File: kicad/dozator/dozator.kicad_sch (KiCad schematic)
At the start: 11 parts, among them J2 LCD: GND 5V SDA SCL, J3 HX711: 5V GND DOUT SCK, SW1 Encoder EC11 H15, U1 Mini-360 5V, U2 DRV8871 MODULE

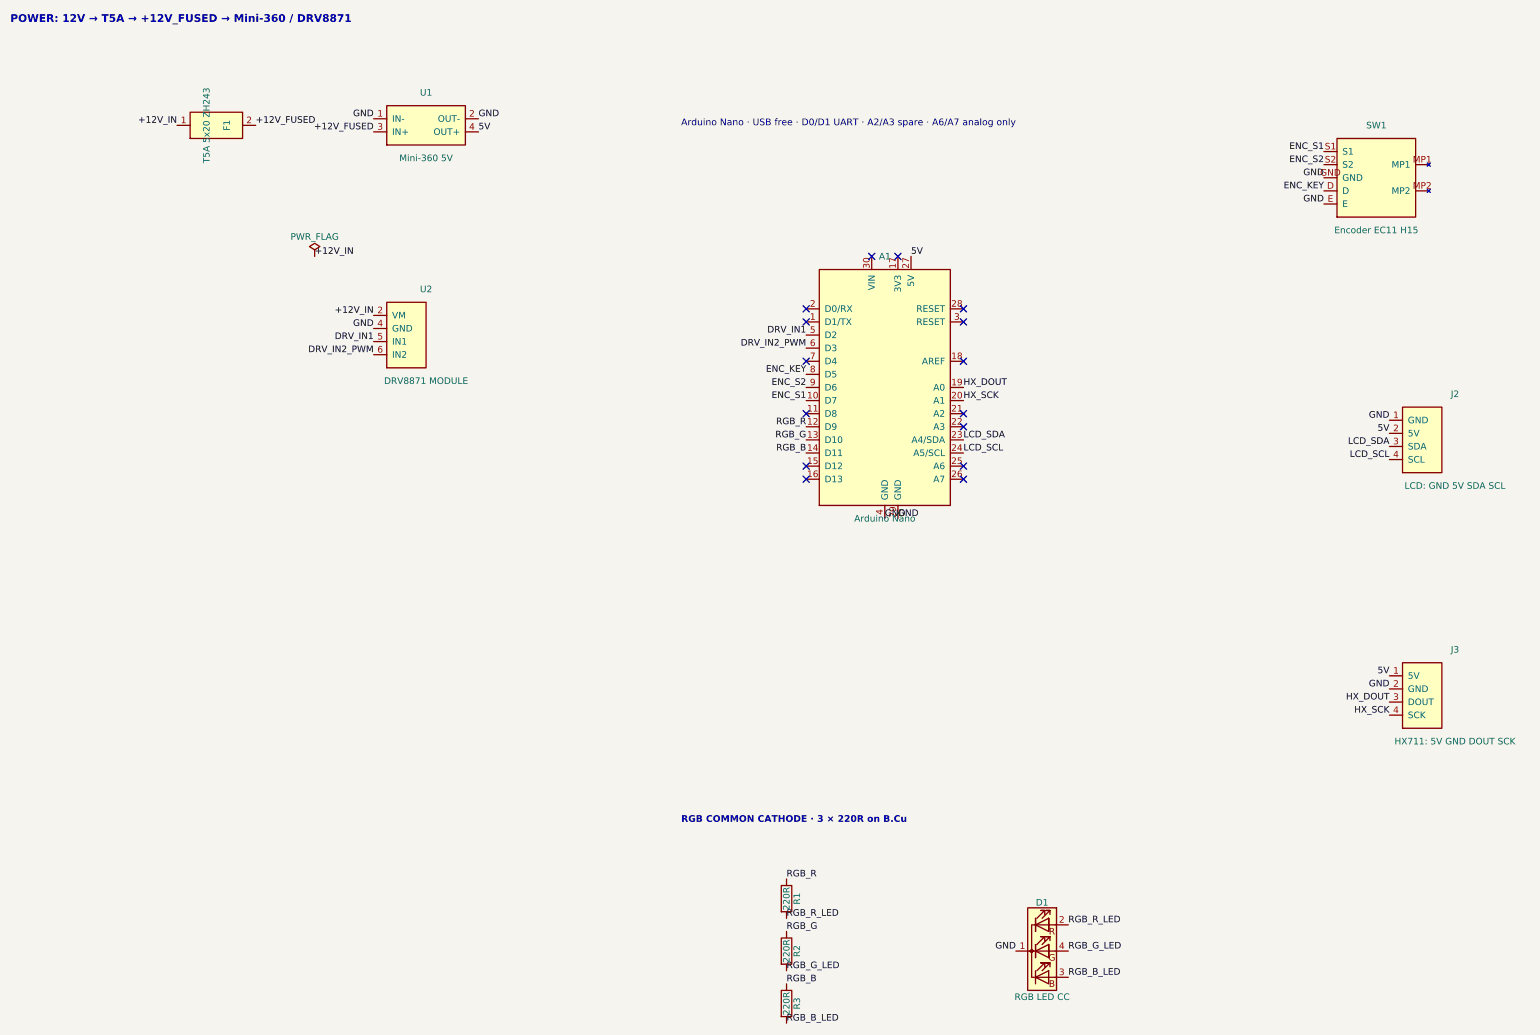
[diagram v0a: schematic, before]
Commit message: Update schematic and add KiCad project
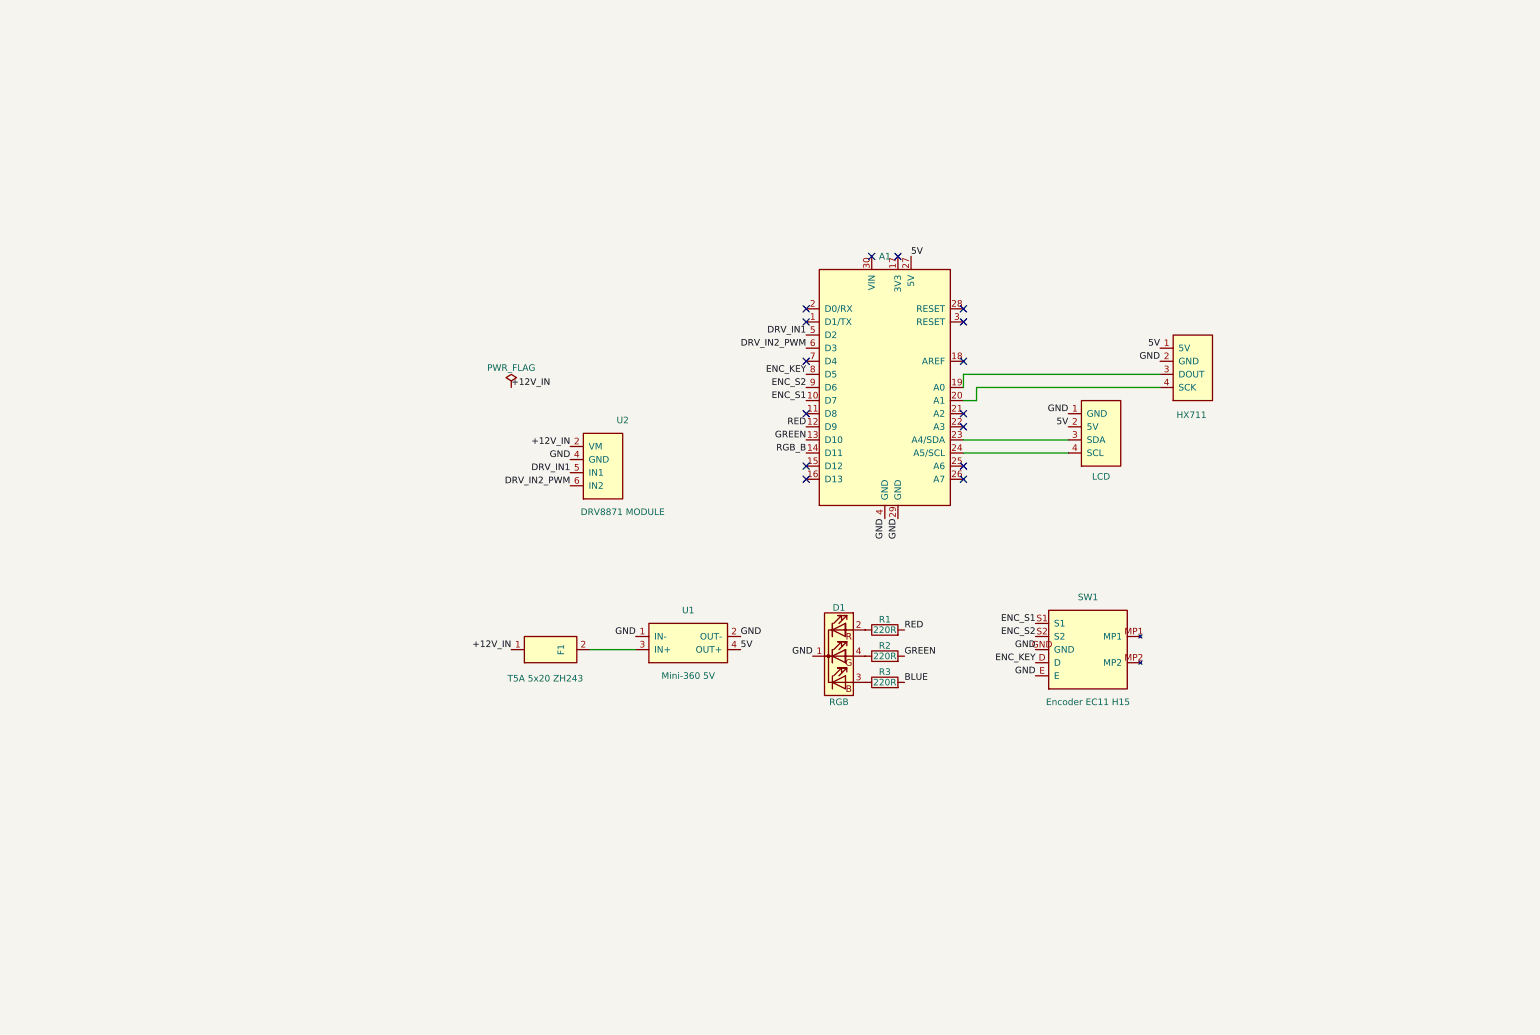
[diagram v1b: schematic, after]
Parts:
- D1: value RGB LED CC -> RGB; footprint LED_THT:LED_D5.0mm-4_RGB -> LED_THT:LED_D5.0mm-4_RGB_Wide_Pins
- J2: value LCD: GND 5V SDA SCL -> LCD
- J3: value HX711: 5V GND DOUT SCK -> HX711
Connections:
- net RGB_B: no longer R3.1
- net +12V_FUSED: no longer names the net of F1.2 (FUSED), U1.3 (IN+)
- net HX_DOUT: no longer names the net of A1.19 (A0), J3.3 (DOUT)
- net HX_SCK: no longer names the net of A1.20 (A1), J3.4 (SCK)
- net LCD_SCL: no longer names the net of A1.24 (A5/SCL), J2.4 (SCL)
- net LCD_SDA: no longer names the net of A1.23 (A4/SDA), J2.3 (SDA)
- net RGB_B_LED: no longer names the net of D1.3 (BA)
- net RGB_B_LED: now also R3.1; no longer R3.2
- net RGB_G: no longer names the net of R2.1
- net RGB_G: now also D1.4 (GA); no longer A1.13 (D10)
- net RGB_G_LED renamed GREEN
- net GREEN: now also A1.13 (D10); no longer D1.4 (GA)
- net RGB_R: no longer names the net of R1.1
- net RGB_R: now also D1.2 (RA); no longer A1.12 (D9)
- net RGB_R_LED renamed RED
- net RED: now also A1.12 (D9); no longer D1.2 (RA)
- new net BLUE: R3.2
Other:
- note removed: "Arduino Nano · USB free · D0/D1 UART · A2/A3 spare · A6/A7 analog only"
- note removed: "POWER: 12V → T5A → +12V_FUSED → Mini-360 / DRV8871"
- note removed: "RGB COMMON CATHODE · 3 × 220R on B.Cu"
- moved on the sheet: D1, F1, R1, R2, R3, SW1, U1, U2
